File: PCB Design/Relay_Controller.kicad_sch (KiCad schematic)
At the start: 51 parts, among them J1 Mains, J2 Conn_0-7, J3 Conn_8, J4 Conn_9, J5 Conn_I2C, J6 Conn_I2C, J7 Conn_Aux, J8 Conn_Sig, U1 AMS1117-3.3, U2 SX1509BIULTRT, U3 TCA9406DC

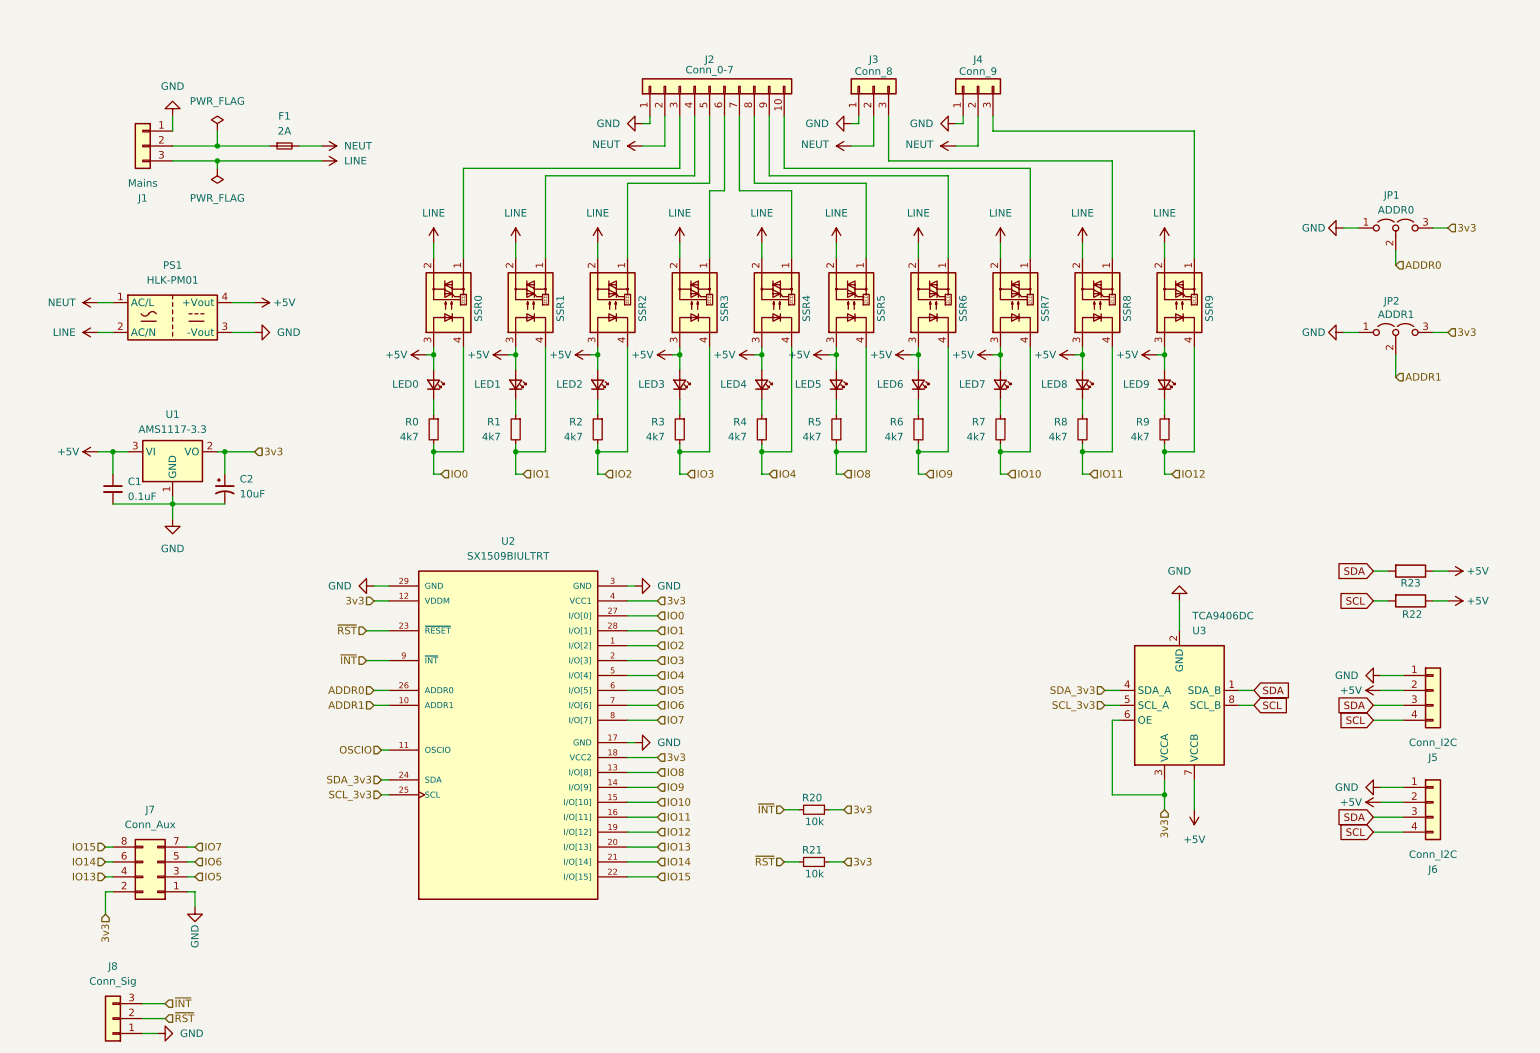
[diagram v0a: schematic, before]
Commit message: Controller Board
Sub board for the controller
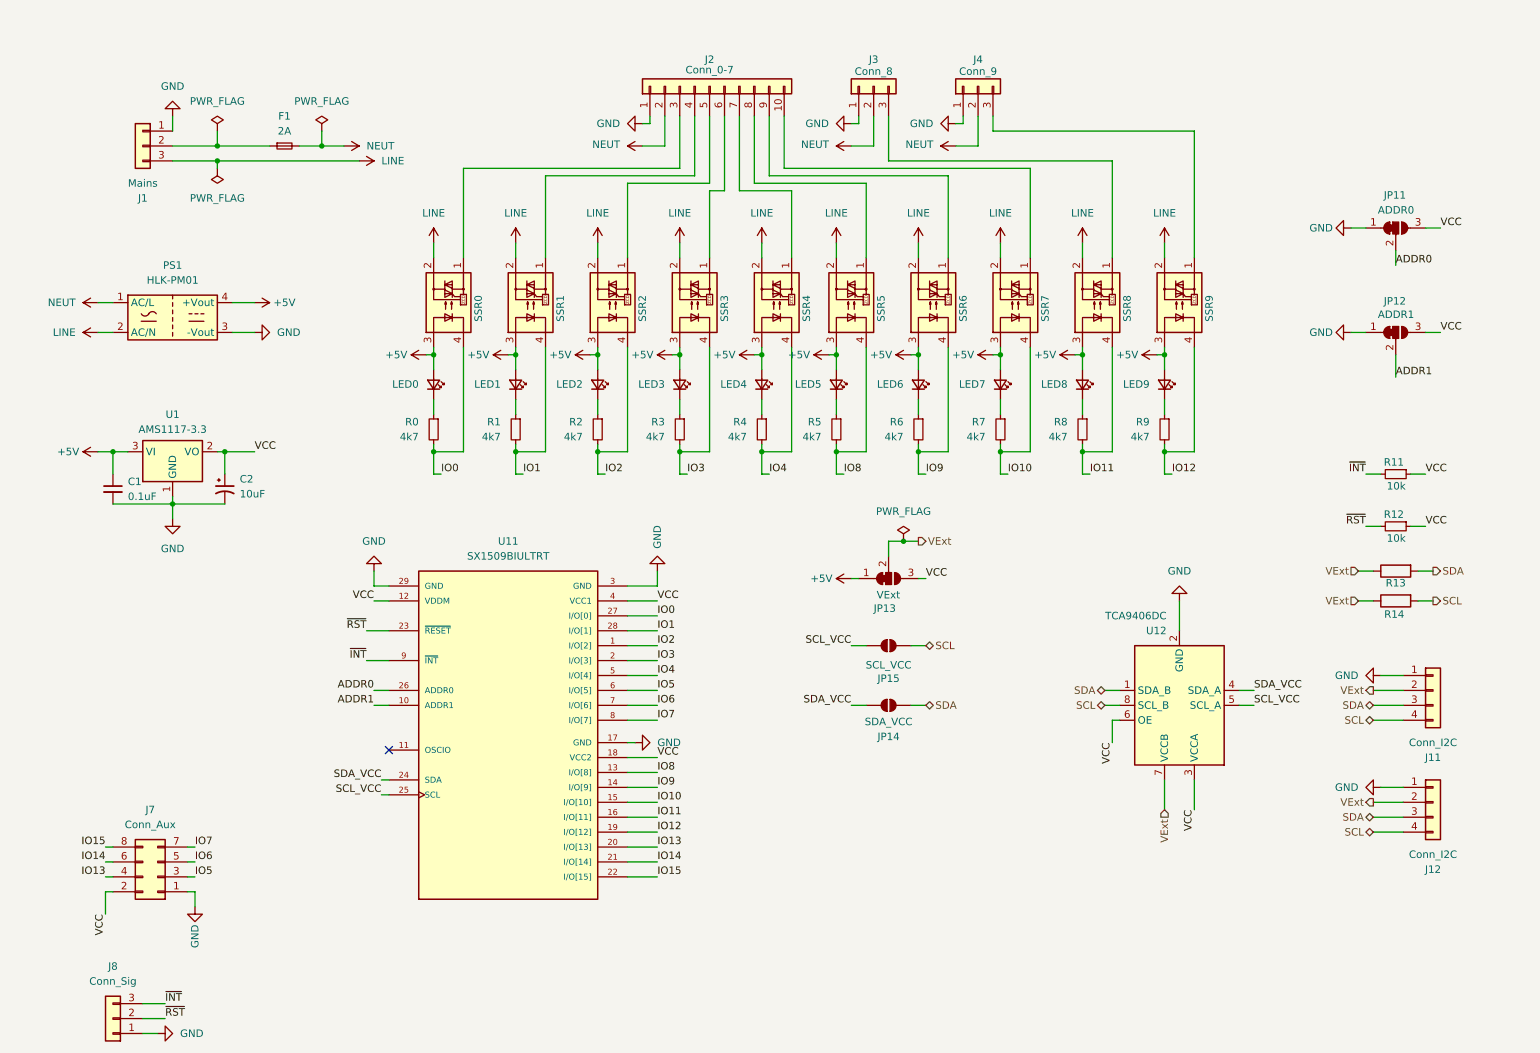
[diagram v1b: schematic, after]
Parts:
- added JP13: VExt, Jumper:SolderJumper-3_P1.3mm_Bridged12_RoundedPad1.0x1.5mm_NumberLabels, symbol Jumper:SolderJumper_3_Bridged12
- added JP14: SDA_VCC, Jumper:SolderJumper-2_P1.3mm_Open_RoundedPad1.0x1.5mm, symbol Jumper:SolderJumper_2_Open
- added JP15: SCL_VCC, Jumper:SolderJumper-2_P1.3mm_Open_RoundedPad1.0x1.5mm, symbol Jumper:SolderJumper_2_Open
- C1, C2: footprint Capacitor_SMD:C_0805_2012Metric -> Capacitor_SMD:C_0805_2012Metric_Pad1.18x1.45mm_HandSolder
- JP11: renamed from JP1; symbol Jumper:Jumper_3_Open -> Jumper:SolderJumper_3_Bridged12; now left out of the parts list
- JP12: renamed from JP2; symbol Jumper:Jumper_3_Open -> Jumper:SolderJumper_3_Bridged12; now left out of the parts list
- U11: renamed from U2; symbol i2c:SX1509BIULTRT -> Vending_Machine:SX1509BIULTRT
- renumbered J5 to J11, J6 to J12, R20 to R11, R21 to R12, R23 to R13, R22 to R14, U3 to U12
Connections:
- net +5V: now also JP13.1 (A); no longer J11.2 (Pin_2), J12.2 (Pin_2), R13.1, R14.1, U12.7 (VCCB)
- net SCL: now also JP15.2 (B)
- net SDA: now also JP14.2 (B)
- net 3v3 renamed VCC
- net VCC: now also JP13.3 (B)
- net OSCIO: no longer names the net of U11.11 (OSCIO)
- net SCL_3v3 renamed SCL_VCC
- net SCL_VCC: now also JP15.1 (A)
- net SDA_3v3 renamed SDA_VCC
- net SDA_VCC: now also JP14.1 (A)
- new net VExt: J11.2 (Pin_2), J12.2 (Pin_2), JP13.2 (C), R13.1, R14.1, U12.7 (VCCB)
- no-connect marks 0 -> 1
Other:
- moved on the sheet: R11, R12, R13, R14, U12

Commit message: Panelize
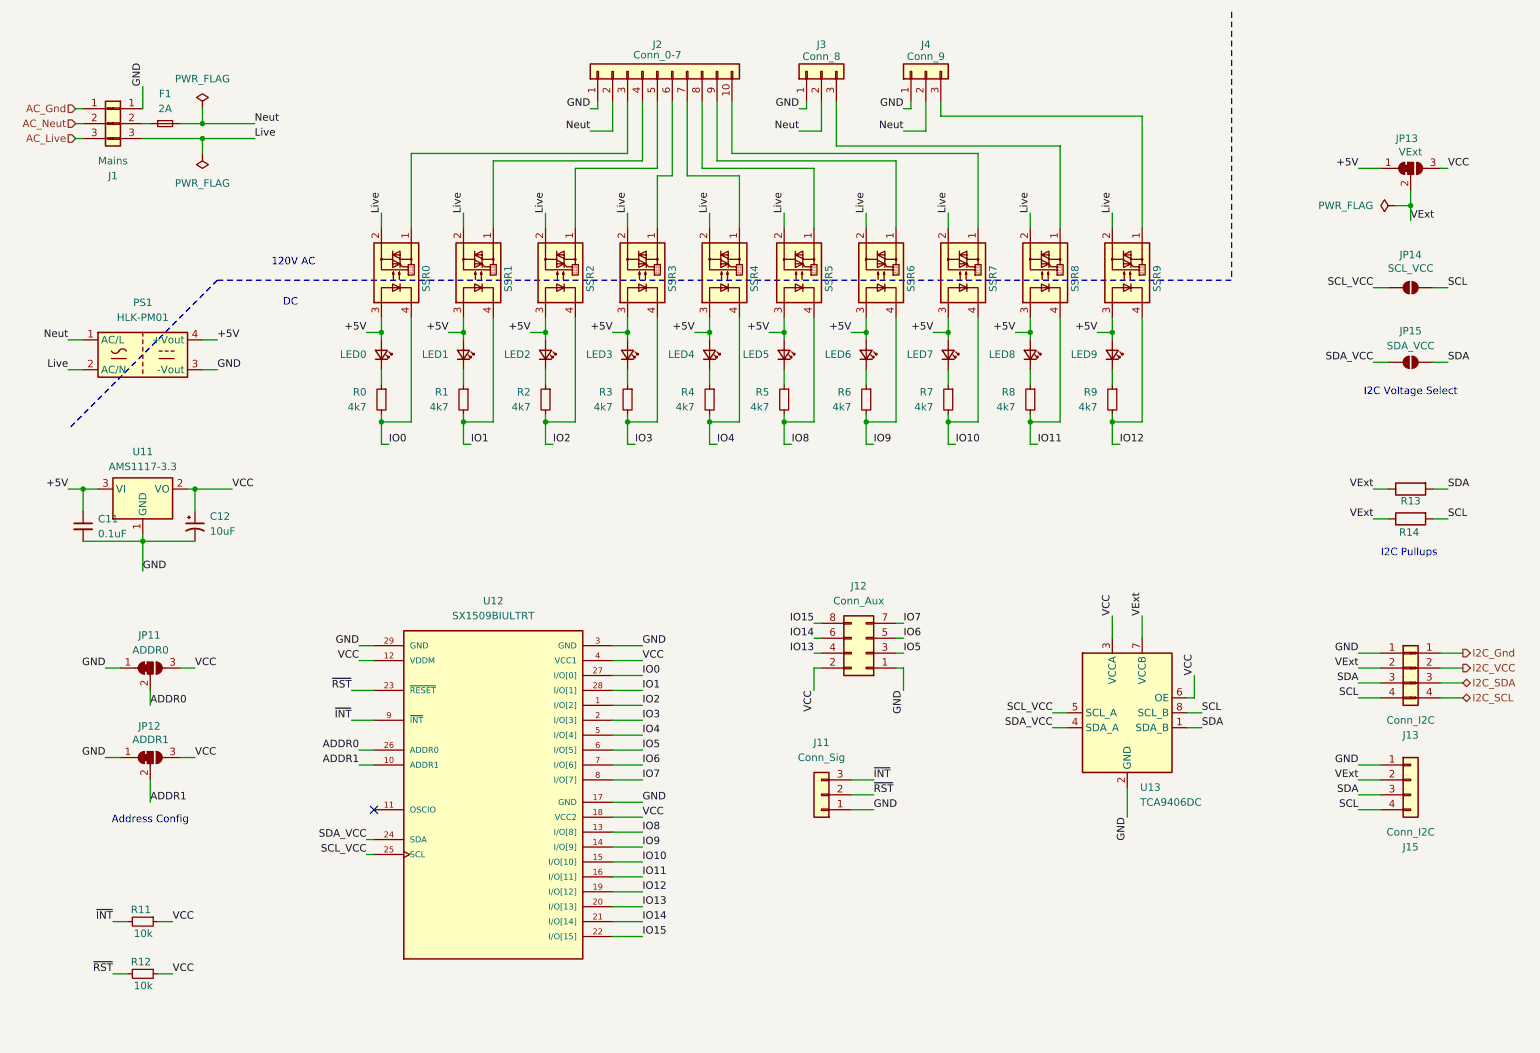
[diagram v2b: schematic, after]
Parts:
- added J14: Conn_01x04_Pin, symbol Connector:Conn_01x04_Pin
- added J41: Conn_01x03_Pin, symbol Connector:Conn_01x03_Pin
- renumbered C1 to C11, C2 to C12, J8 to J11, J7 to J12, J11 to J13, J12 to J15, JP15 to JP14, JP14 to JP15, U1 to U11, U11 to U12, U12 to U13
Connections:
- net LINE renamed Live
- net NEUT renamed Neut
- new net AC_Gnd: J41.1 (Pin_1)
- new net AC_Live: J41.3 (Pin_3)
- new net AC_Neut: J41.2 (Pin_2)
- new net I2C_Gnd: J14.1 (Pin_1)
- new net I2C_SCL: J14.4 (Pin_4)
- new net I2C_SDA: J14.3 (Pin_3)
- new net I2C_VCC: J14.2 (Pin_2)
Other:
- note added: "120V AC"
- note added: "Address Config"
- note added: "DC"
- note added: "I2C Pullups"
- note added: "I2C Voltage Select"
- moved on the sheet: C11, C12, F1, J1, J11, J12, J13, J15, J2, J3, J4, JP11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

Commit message: Added Multiplexer
Added separate IO Multiplexer breakout
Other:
- title: I2C Relay Controler -> Relay Controller
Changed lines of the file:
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@@
 	(paper "A4")
 	(title_block
-		(title "I2C Relay Controler")
+		(title "Relay Controller")
 		(date "2024-03-19")
 		(rev "2")

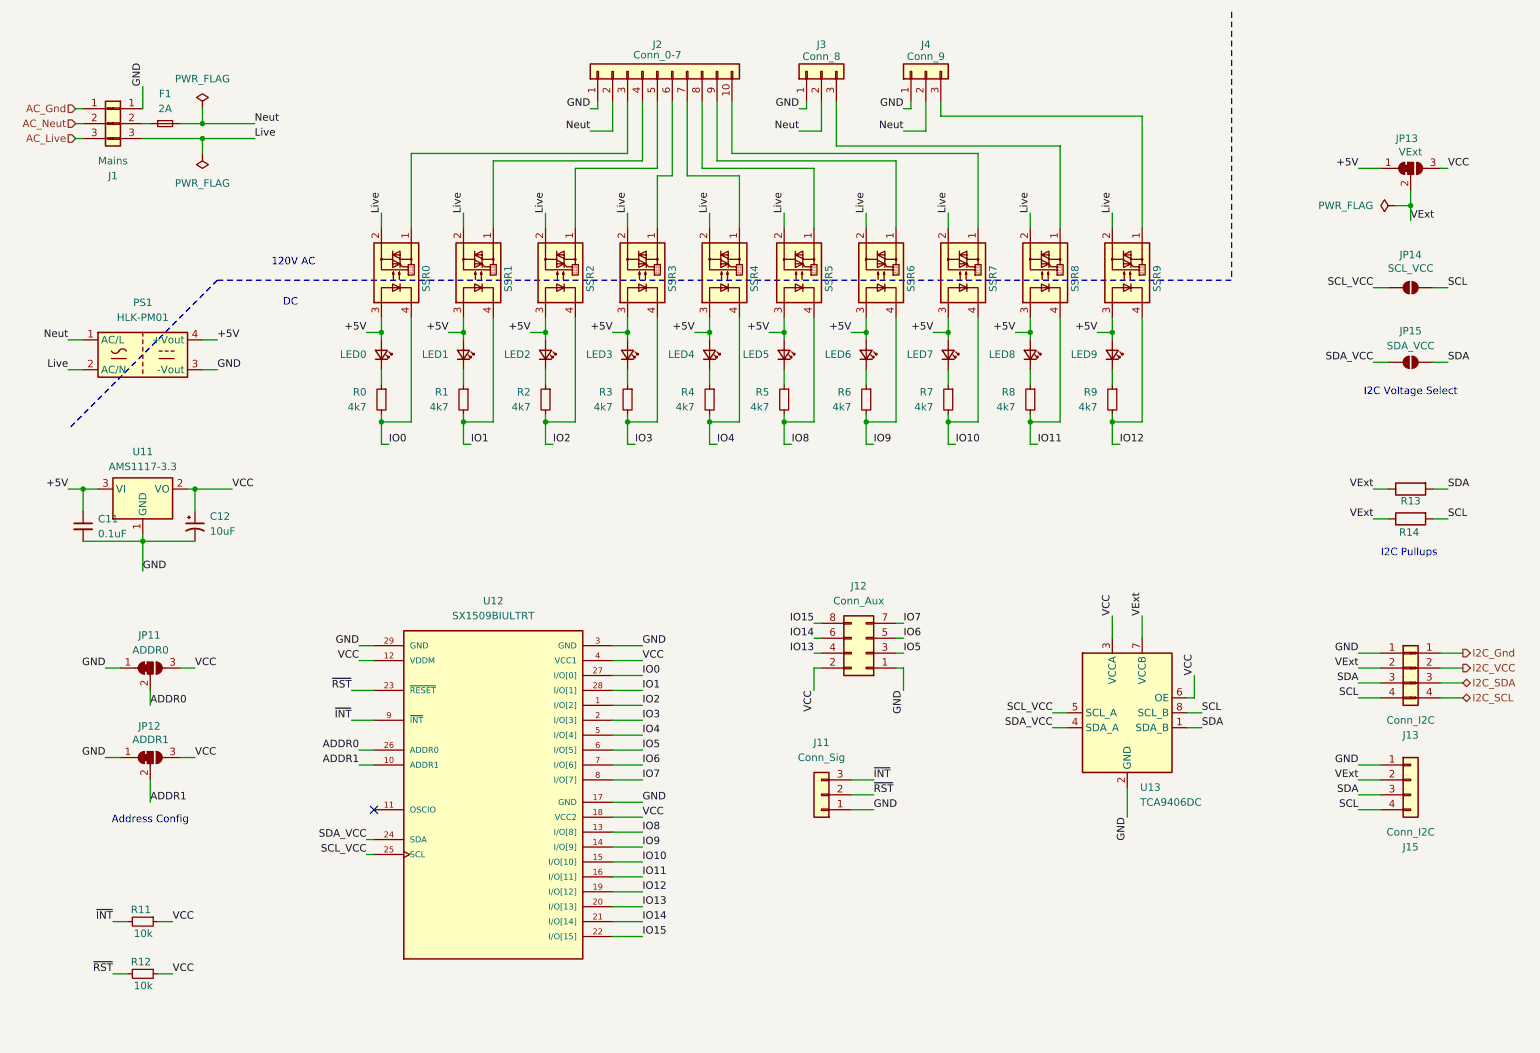
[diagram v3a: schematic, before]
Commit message: Tweaks and Updates
Added OSCIO pin to breakout board.
A few more tweaks
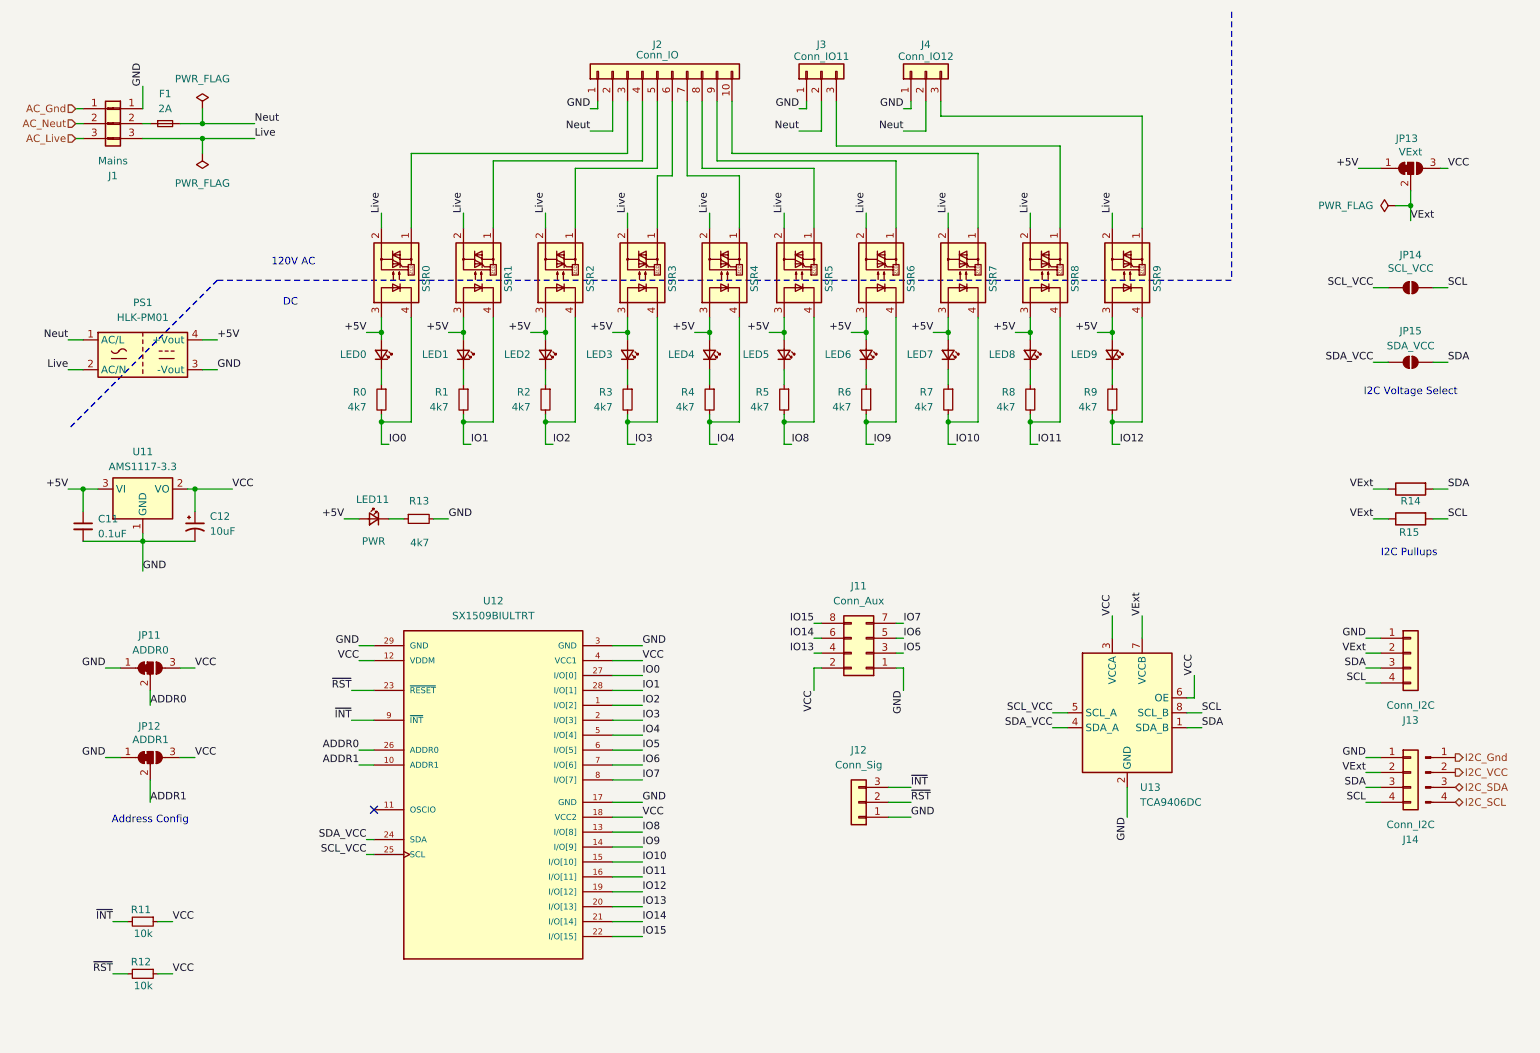
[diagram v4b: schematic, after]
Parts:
- added LED11: PWR, LED_SMD:LED_0805_2012Metric_Pad1.15x1.40mm_HandSolder, symbol Device:LED_Small
- added R13: 4k7, Resistor_SMD:R_0805_2012Metric_Pad1.20x1.40mm_HandSolder, symbol Device:R_Small
- J2: value Conn_0-7 -> Conn_IO
- J3: value Conn_8 -> Conn_IO11
- J4: value Conn_9 -> Conn_IO12
- renumbered J12 to J11, J11 to J12, J15 to J13, J13 to J14, J14 to J15, R13 to R14, R14 to R15
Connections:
- net +5V: now also LED11.2 (A)
- net GND: now also R13.2
- new net: LED11.1 (K), R13.1
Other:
- moved on the sheet: J12, J13, J14
